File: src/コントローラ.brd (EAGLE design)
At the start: 100 x 80 mm, 13 parts, among them SW1 TOGGLESWITCH

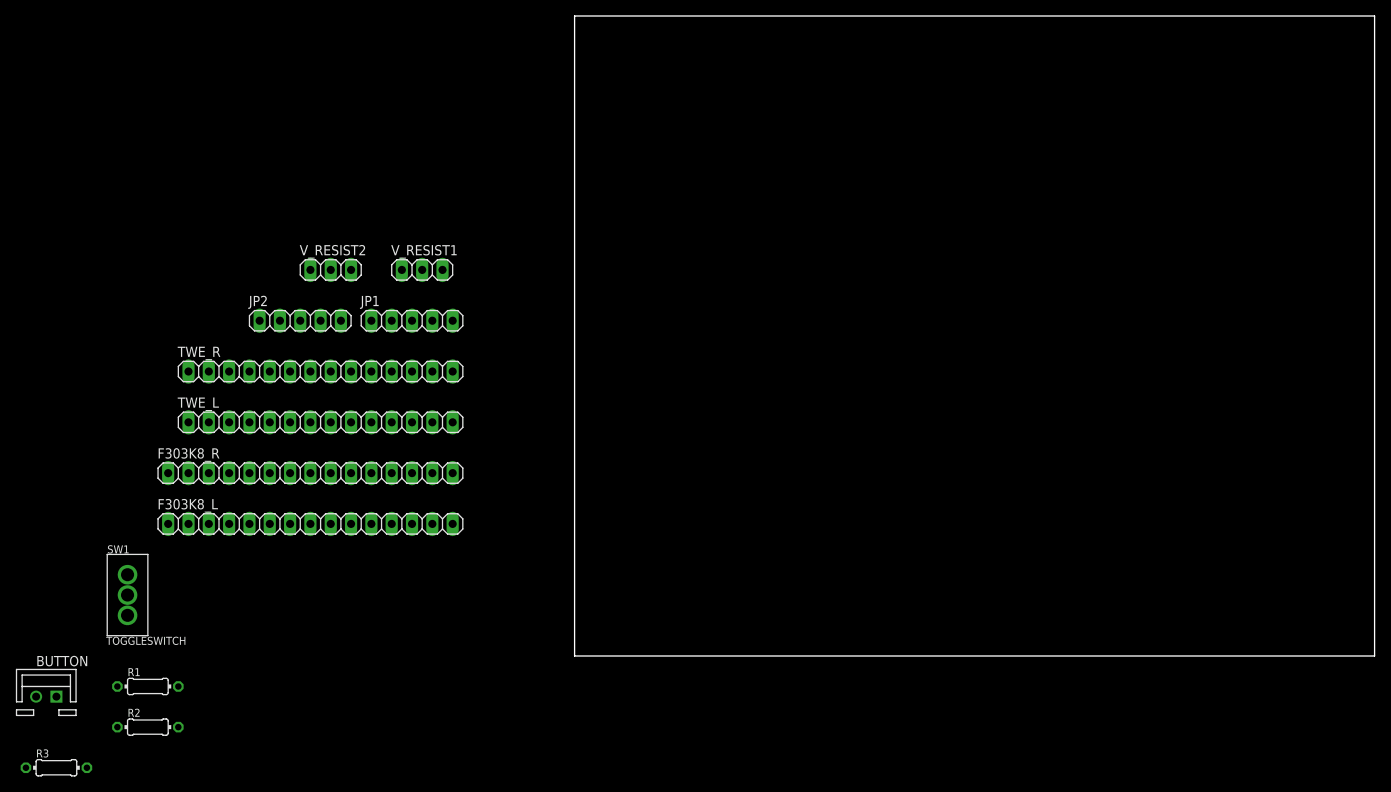
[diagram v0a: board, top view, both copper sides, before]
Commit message: [add]コントローラー.brdの追加
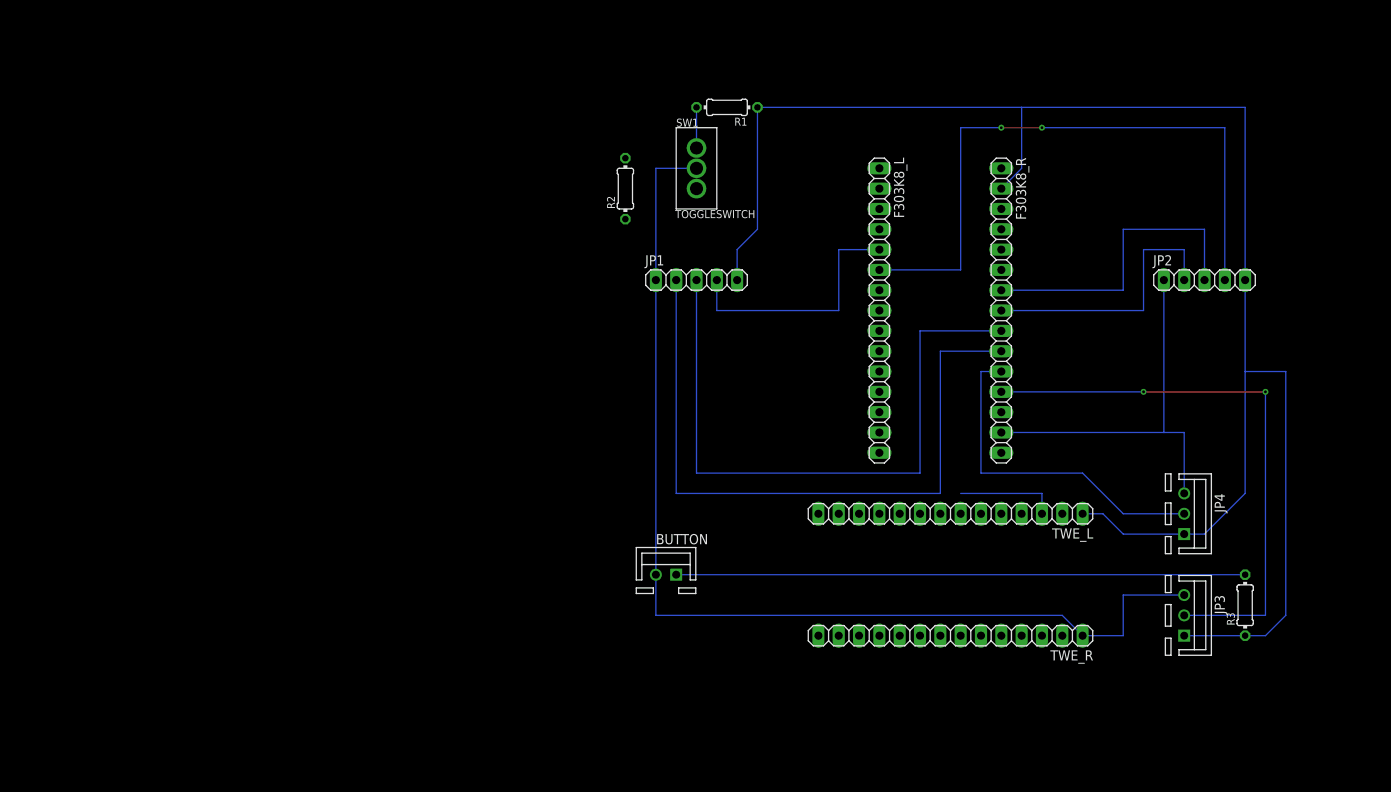
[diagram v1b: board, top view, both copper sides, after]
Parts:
- removed V_RESIST1, V_RESIST2: (no value), pinhead:1X03
- added JP3, JP4: (no value), con-jst-xh:B3B-XH
- added U$1: (no value), prototyping-board:TYPE.B
- moved R3 150.0 mm to (83.8, 6.35), turned to 90 degrees
- moved JP2 113.1 mm to (78.7, 47.0)
- moved R1 102.4 mm to (19.1, 68.6), turned to 180 degrees
- moved R2 90.0 mm to (6.35, 58.4), turned to 90 degrees
- moved SW1 88.9 mm to (15.2, 61.0)
- moved F303K8_R 88.7 mm to (53.3, 43.2), turned to 270 degrees
- moved TWE_R 85.4 mm to (47.0, 2.54), turned to 180 degrees
- moved TWE_L 79.6 mm to (47.0, 17.8), turned to 180 degrees
- moved BUTTON 79.0 mm to (11.4, 10.2)
- moved F303K8_L 76.0 mm to (38.1, 43.2), turned to 270 degrees
- moved JP1 35.9 mm to (15.2, 47.0)
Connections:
- net 3V3: now also JP3.3, JP4.3; no longer V_RESIST1.1, V_RESIST2.1
- net BT_IN: now also F303K8_L.9
- net GND: now also JP3.1, JP4.1; no longer V_RESIST1.3, V_RESIST2.3
- net SW_DOWN: now also F303K8_L.11
- net SW_UP: now also F303K8_L.10
- net VR_IN1: now also JP3.2; no longer V_RESIST1.2
- net VR_IN2: now also JP4.2; no longer V_RESIST2.2
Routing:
- net GND: track 0.00 -> 215.9 mm
- net 3V3: track 0.00 -> 182.7 mm
- net VERT1: track 0.00 -> 85.1 mm
- net SEL2: track 0.00 -> 80.0 mm, vias 0 -> 2
- net HORZ1: track 0.00 -> 80.0 mm
- net VR_IN1: track 0.00 -> 71.1 mm, vias 0 -> 2
- net BT_IN: track 0.00 -> 71.1 mm
- net VR_IN2: track 0.00 -> 42.7 mm
- net HORZ2: track 0.00 -> 39.4 mm
- net VERT2: track 0.00 -> 34.3 mm
- net SEL1: track 0.00 -> 31.8 mm
- net TX: track 0.00 -> 12.7 mm
- net SW_UP: track 0.00 -> 5.08 mm
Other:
- board outline removed

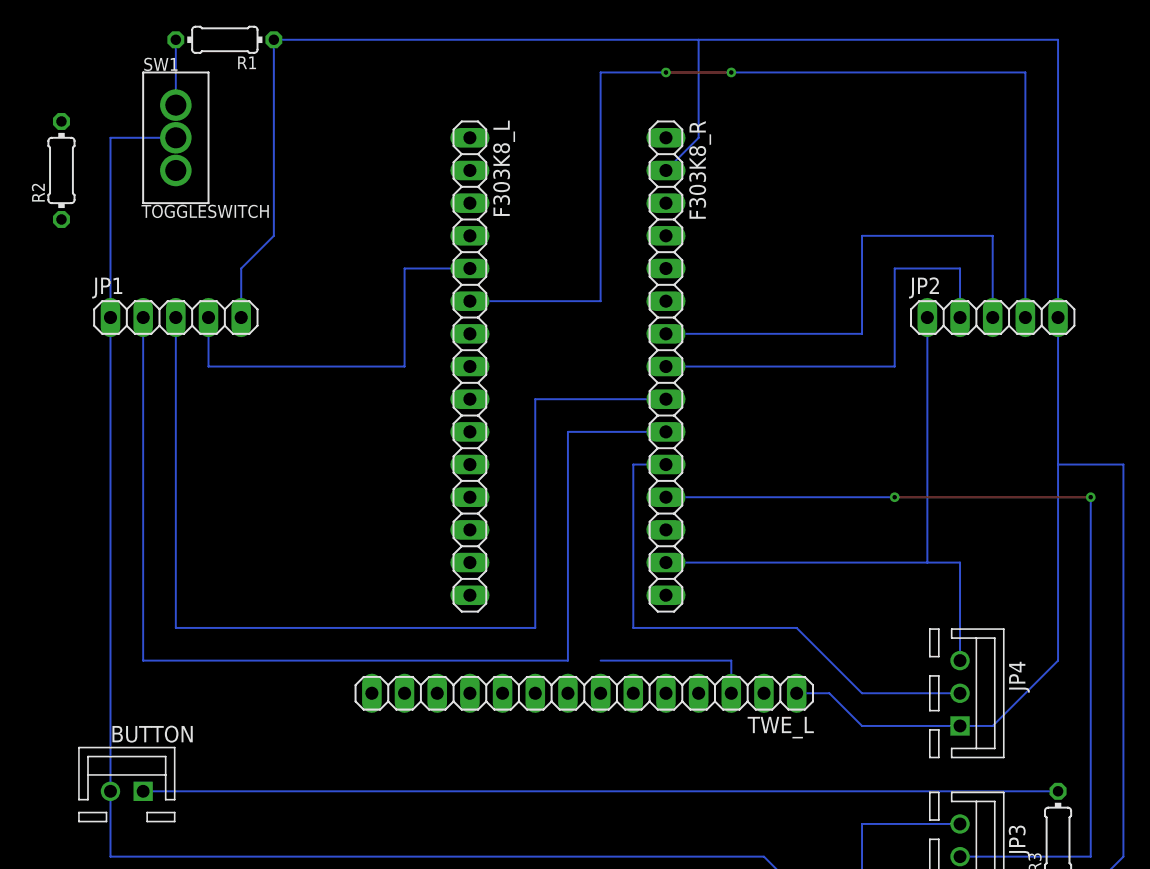
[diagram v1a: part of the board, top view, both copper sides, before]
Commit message: [fix]コントローラー.brdの修正
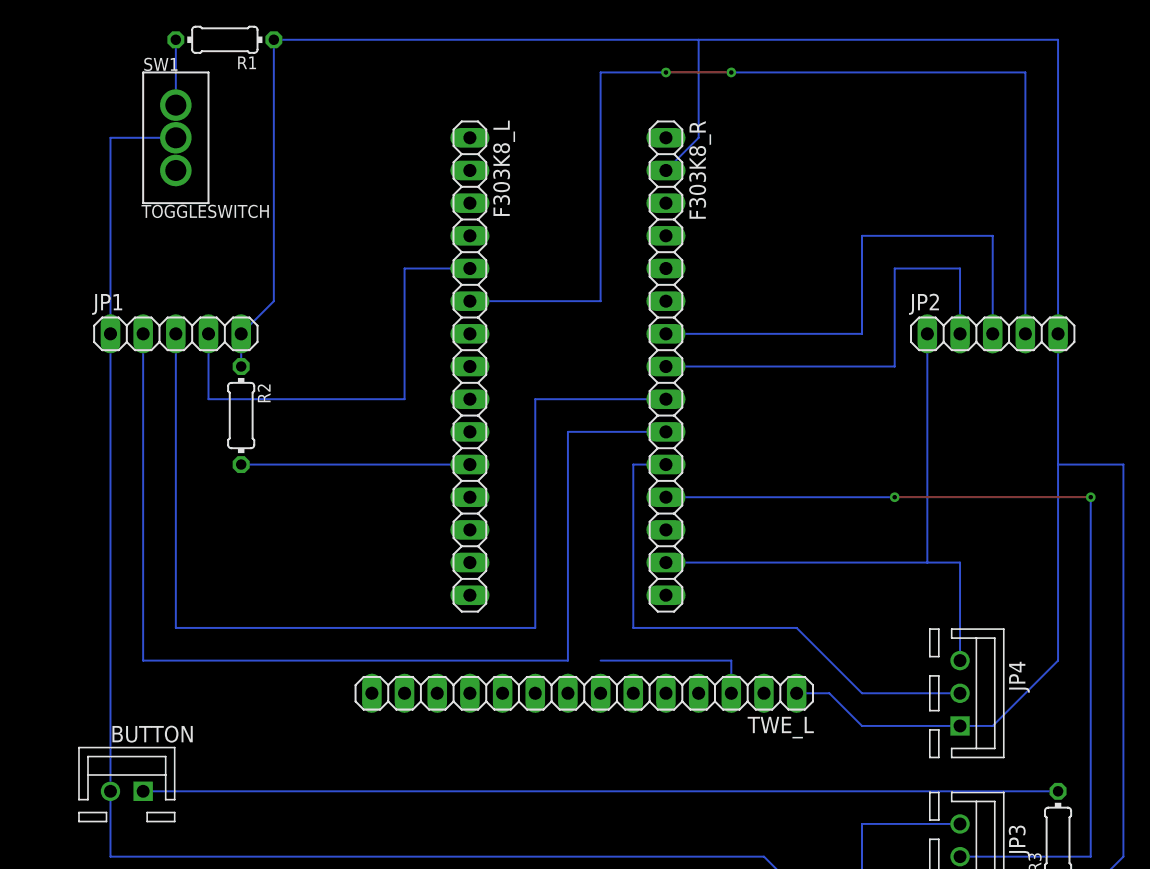
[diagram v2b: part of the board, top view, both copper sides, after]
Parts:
- moved R2 23.6 mm to (20.3, 39.4), turned to 270 degrees
- moved JP1 1.27 mm to (15.2, 45.7)
- moved JP2 1.27 mm to (78.7, 45.7)
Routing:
- net SW_DOWN: track 0.00 -> 17.8 mm
- net SEL1: track 31.8 -> 35.6 mm
- net GND: track 215.9 -> 219.7 mm
- net VERT1: track 85.1 -> 83.8 mm
- net 3V3: track 182.7 -> 181.4 mm
- net VERT2: track 34.3 -> 35.6 mm
- net HORZ2: track 39.4 -> 40.6 mm
- net SEL2: track 80.0 -> 81.3 mm
- net HORZ1: track 80.0 -> 78.7 mm
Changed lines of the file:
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@@
 <attribute name="VALUE" x="50.165" y="62.23" size="1.27" layer="27" rot="R270"/>
 </element>
-<element name="JP1" library="pinhead" library_urn="urn:adsk.eagle:library:325" package="1X05" package3d_urn="urn:adsk.eagle:package:22469/2" value="" x="15.24" y="46.99" smashed="yes">
-<attribute name="NAME" x="8.8138" y="48.8188" size="1.27" layer="25" ratio="10"/>
-<attribute name="POPULARITY" value="69" x="35.56" y="5.08" size="1.778" layer="27" display="off"/>
-<attribute name="VALUE" x="8.89" y="43.815" size="1.27" layer="27"/>
-</element>
-<element name="JP2" library="pinhead" library_urn="urn:adsk.eagle:library:325" package="1X05" package3d_urn="urn:adsk.eagle:package:22469/2" value="" x="78.74" y="46.99" smashed="yes">
-<attribute name="NAME" x="72.3138" y="48.8188" size="1.27" layer="25" ratio="10"/>
-<attribute name="POPULARITY" value="69" x="113.03" y="5.08" size="1.778" layer="27" display="off"/>
-<attribute name="VALUE" x="72.39" y="43.815" size="1.27" layer="27"/>
+<element name="JP1" library="pinhead" library_urn="urn:adsk.eagle:library:325" package="1X05" package3d_urn="urn:adsk.eagle:package:22469/2" value="" x="15.24" y="45.72" smashed="yes">
+<attribute name="NAME" x="8.8138" y="47.5488" size="1.27" layer="25" ratio="10"/>
+<attribute name="POPULARITY" value="69" x="35.56" y="3.81" size="1.778" layer="27" display="off"/>
+<attribute name="VALUE" x="8.89" y="42.545" size="1.27" layer="27"/>
+</element>
+<element name="JP2" library="pinhead" library_urn="urn:adsk.eagle:library:325" package="1X05" package3d_urn="urn:adsk.eagle:package:22469/2" value="" x="78.74" y="45.72" smashed="yes">
+<attribute name="NAME" x="72.3138" y="47.5488" size="1.27" layer="25" ratio="10"/>
+<attribute name="POPULARITY" value="69" x="113.03" y="3.81" size="1.778" layer="27" display="off"/>
+<attribute name="VALUE" x="72.39" y="42.545" size="1.27" layer="27"/>
 </element>
 <element name="TWE_L" library="pinhead" library_urn="urn:adsk.eagle:library:325" package="1X14" package3d_urn="urn:adsk.eagle:package:22417/2" value="" x="46.99" y="17.78" smashed="yes" rot="R180">
@@
 <attribute name="VALUE" x="20.6756" y="69.0626" size="0.9906" layer="27" ratio="10" rot="R180"/>
 </element>
-<element name="R2" library="rcl" library_urn="urn:adsk.eagle:library:334" package="0204/7" package3d_urn="urn:adsk.eagle:package:23498/2" value="10k" x="6.35" y="58.42" smashed="yes" rot="R90">
-<attribute name="NAME" x="5.0546" y="55.88" size="0.9906" layer="25" ratio="10" rot="R90"/>
-<attribute name="POPULARITY" value="79" x="6.35" y="58.42" size="1.778" layer="27" rot="R90" display="off"/>
-<attribute name="SPICEPREFIX" value="R" x="6.35" y="58.42" size="1.778" layer="27" rot="R90" display="off"/>
-<attribute name="VALUE" x="6.8326" y="56.7944" size="0.9906" layer="27" ratio="10" rot="R90"/>
+<element name="R2" library="rcl" library_urn="urn:adsk.eagle:library:334" package="0204/7" package3d_urn="urn:adsk.eagle:package:23498/2" value="10k" x="20.32" y="39.37" smashed="yes" rot="R270">
+<attribute name="NAME" x="21.6154" y="41.91" size="0.9906" layer="25" ratio="10" rot="R270"/>
+<attribute name="POPULARITY" value="79" x="20.32" y="39.37" size="1.778" layer="27" rot="R270" display="off"/>
+<attribute name="SPICEPREFIX" value="R" x="20.32" y="39.37" size="1.778" layer="27" rot="R270" display="off"/>
+<attribute name="VALUE" x="19.8374" y="40.9956" size="0.9906" layer="27" ratio="10" rot="R270"/>
 </element>
 <element name="BUTTON" library="con-jst-xh" package="B2B-XH" value="02-JST" x="11.43" y="10.16" smashed="yes">
@@
 <wire x1="83.82" y1="20.32" x2="78.74" y2="15.24" width="0.1524" layer="16"/>
 <wire x1="78.74" y1="15.24" x2="76.2" y2="15.24" width="0.1524" layer="16"/>
-<wire x1="22.86" y1="68.58" x2="22.86" y2="53.34" width="0.1524" layer="16"/>
-<wire x1="22.86" y1="53.34" x2="20.32" y2="50.8" width="0.1524" layer="16"/>
-<wire x1="20.32" y1="50.8" x2="20.32" y2="46.99" width="0.1524" layer="16"/>
 <wire x1="22.86" y1="68.58" x2="55.88" y2="68.58" width="0.1524" layer="16"/>
 <wire x1="55.88" y1="68.58" x2="83.82" y2="68.58" width="0.1524" layer="16"/>
-<wire x1="83.82" y1="68.58" x2="83.82" y2="46.99" width="0.1524" layer="16"/>
+<wire x1="83.82" y1="68.58" x2="83.82" y2="45.72" width="0.1524" layer="16"/>
 <wire x1="53.34" y1="58.42" x2="55.88" y2="60.96" width="0.1524" layer="16"/>
 <wire x1="55.88" y1="60.96" x2="55.88" y2="68.58" width="0.1524" layer="16"/>
@@
 <wire x1="88.9" y1="5.08" x2="88.9" y2="35.56" width="0.1524" layer="16"/>
 <wire x1="88.9" y1="35.56" x2="83.82" y2="35.56" width="0.1524" layer="16"/>
-<wire x1="83.82" y1="46.99" x2="83.82" y2="35.56" width="0.1524" layer="16"/>
-<wire x1="6.35" y1="54.61" x2="20.32" y2="46.99" width="0" layer="19" extent="1-1"/>
+<wire x1="83.82" y1="45.72" x2="83.82" y2="35.56" width="0.1524" layer="16"/>
+<wire x1="20.32" y1="45.72" x2="20.32" y2="43.18" width="0.1524" layer="16"/>
+<wire x1="20.32" y1="45.72" x2="22.86" y2="48.26" width="0.1524" layer="16"/>
+<wire x1="22.86" y1="48.26" x2="22.86" y2="68.58" width="0.1524" layer="16"/>
 </signal>
 <signal name="3V3">
@@
 <contactref element="JP3" pad="3"/>
 <contactref element="JP4" pad="3"/>
-<wire x1="10.16" y1="10.16" x2="10.16" y2="46.99" width="0.1524" layer="16"/>
-<wire x1="10.16" y1="46.99" x2="10.16" y2="60.96" width="0.1524" layer="16"/>
+<wire x1="10.16" y1="10.16" x2="10.16" y2="45.72" width="0.1524" layer="16"/>
+<wire x1="10.16" y1="45.72" x2="10.16" y2="60.96" width="0.1524" layer="16"/>
 <wire x1="10.16" y1="60.96" x2="15.24" y2="60.96" width="0.1524" layer="16"/>
 <wire x1="76.2" y1="20.32" x2="76.2" y2="27.94" width="0.1524" layer="16"/>
 <wire x1="76.2" y1="27.94" x2="73.66" y2="27.94" width="0.1524" layer="16"/>
 <wire x1="73.66" y1="27.94" x2="53.34" y2="27.94" width="0.1524" layer="16"/>
-<wire x1="73.66" y1="46.99" x2="73.66" y2="27.94" width="0.1524" layer="16"/>
+<wire x1="73.66" y1="45.72" x2="73.66" y2="27.94" width="0.1524" layer="16"/>
 <wire x1="63.5" y1="2.54" x2="68.58" y2="2.54" width="0.1524" layer="16"/>
 <wire x1="68.58" y1="2.54" x2="68.58" y2="7.62" width="0.1524" layer="16"/>
@@
 <wire x1="71.12" y1="43.18" x2="71.12" y2="50.8" width="0.1524" layer="16"/>
 <wire x1="71.12" y1="50.8" x2="76.2" y2="50.8" width="0.1524" layer="16"/>
-<wire x1="76.2" y1="50.8" x2="76.2" y2="46.99" width="0.1524" layer="16"/>
+<wire x1="76.2" y1="50.8" x2="76.2" y2="45.72" width="0.1524" layer="16"/>
 </signal>
 <signal name="HORZ2">
@@
 <wire x1="68.58" y1="45.72" x2="68.58" y2="53.34" width="0.1524" layer="16"/>
 <wire x1="68.58" y1="53.34" x2="78.74" y2="53.34" width="0.1524" layer="16"/>
-<wire x1="78.74" y1="53.34" x2="78.74" y2="46.99" width="0.1524" layer="16"/>
+<wire x1="78.74" y1="53.34" x2="78.74" y2="45.72" width="0.1524" layer="16"/>
 </signal>
 <signal name="SEL2">
 <contactref element="JP2" pad="4"/>
 <contactref element="F303K8_L" pad="6"/>
-<wire x1="81.28" y1="46.99" x2="81.28" y2="66.04" width="0.1524" layer="16"/>
+<wire x1="81.28" y1="45.72" x2="81.28" y2="66.04" width="0.1524" layer="16"/>
 <wire x1="81.28" y1="66.04" x2="58.42" y2="66.04" width="0.1524" layer="16"/>
 <via x="58.42" y="66.04" extent="1-16" drill="0.35"/>
@@
 <contactref element="JP1" pad="2"/>
 <contactref element="F303K8_R" pad="10"/>
-<wire x1="12.7" y1="46.99" x2="12.7" y2="20.32" width="0.1524" layer="16"/>
+<wire x1="12.7" y1="45.72" x2="12.7" y2="20.32" width="0.1524" layer="16"/>
 <wire x1="12.7" y1="20.32" x2="45.72" y2="20.32" width="0.1524" layer="16"/>
 <wire x1="45.72" y1="20.32" x2="45.72" y2="38.1" width="0.1524" layer="16"/>
@@
 <contactref element="JP1" pad="3"/>
 <contactref element="F303K8_R" pad="9"/>
-<wire x1="15.24" y1="46.99" x2="15.24" y2="22.86" width="0.1524" layer="16"/>
+<wire x1="15.24" y1="45.72" x2="15.24" y2="22.86" width="0.1524" layer="16"/>
 <wire x1="15.24" y1="22.86" x2="43.18" y2="22.86" width="0.1524" layer="16"/>
 <wire x1="43.18" y1="22.86" x2="43.18" y2="40.64" width="0.1524" layer="16"/>
@@
 <contactref element="JP1" pad="4"/>
 <contactref element="F303K8_L" pad="5"/>
-<wire x1="17.78" y1="46.99" x2="17.78" y2="43.18" width="0.1524" layer="16"/>
-<wire x1="17.78" y1="43.18" x2="33.02" y2="43.18" width="0.1524" layer="16"/>
-<wire x1="33.02" y1="43.18" x2="33.02" y2="50.8" width="0.1524" layer="16"/>
+<wire x1="17.78" y1="45.72" x2="17.78" y2="40.64" width="0.1524" layer="16"/>
+<wire x1="17.78" y1="40.64" x2="33.02" y2="40.64" width="0.1524" layer="16"/>
+<wire x1="33.02" y1="40.64" x2="33.02" y2="50.8" width="0.1524" layer="16"/>
 <wire x1="33.02" y1="50.8" x2="38.1" y2="50.8" width="0.1524" layer="16"/>
 </signal>
@@
 <contactref element="R2" pad="2"/>
 <contactref element="F303K8_L" pad="11"/>
-<wire x1="38.1" y1="35.56" x2="6.35" y2="62.23" width="0" layer="19" extent="1-1"/>
-<wire x1="15.24" y1="58.42" x2="38.1" y2="35.56" width="0" layer="19" extent="1-1"/>
+<wire x1="20.32" y1="35.56" x2="38.1" y2="35.56" width="0.1524" layer="16"/>
+<wire x1="20.32" y1="35.56" x2="15.24" y2="58.42" width="0" layer="19" extent="1-1"/>
 </signal>
 <signal name="BT_IN">

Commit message: [add]メイン回路
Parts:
- moved F303K8_L 2.54 mm to (38.1, 45.7)
- moved F303K8_R 2.54 mm to (53.3, 45.7)
- moved JP1 2.54 mm to (15.2, 48.3)
- moved R2 2.54 mm to (20.3, 41.9)
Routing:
- net BT_IN: track 71.1 -> 129.5 mm, vias 0 -> 2
- net SW_UP: track 5.08 -> 50.8 mm, vias 0 -> 2
- net TX: track 12.7 -> 48.3 mm, vias 0 -> 2
- net RX: track 0.00 -> 33.0 mm, vias 0 -> 2
- net SW_DOWN: track 17.8 -> 45.7 mm, vias 0 -> 2
- net 3V3: track 181.4 -> 204.3 mm, vias 0 -> 2
- net GND: track 219.7 -> 224.3 mm
- net SEL2: track 81.3 -> 78.7 mm
- net VR_IN2: track 42.7 -> 45.3 mm
- net VERT2: track 35.6 -> 33.0 mm
- net HORZ2: track 40.6 -> 38.1 mm
- net VR_IN1: track 71.1 -> 73.7 mm

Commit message: fix
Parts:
- added BUTTON2: 02-JST, con-jst-xh:B2B-XH
- added KAHEN: (no value), pinhead:1X03
- added R4, R5, R6: 10k, rcl:0204/7
- added R7, R8, R9: (no value), rcl:0207/7
- added SLIDESWITCH: SLEDESWITCH, slide switch:SLIDESWITCH
- added SW2: TOGGLESWITCH, ToggleSwitch:TOGGLESWITCH
- moved R3 83.9 mm to (3.81, -19.1), turned to 0 degrees
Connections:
- net SW_DOWN renamed SW_DOWN1
- net SW_UP renamed SW_UP1
- removed net BT_IN: BUTTON.1, F303K8_L.9, R3.2
- new net BT_IN1: BUTTON.1, F303K8_L.9, R5.2
- new net BT_IN2: F303K8_L.14, R6.2
- new net CONNECT: SLIDESWITCH.1
- new net CONNECT1: SLIDESWITCH.2
- new net N$1: R7.2, SLIDESWITCH.5
- new net N$2: R8.2, SLIDESWITCH.6
- new net N$5: KAHEN.2
- new net N$7: R9.1
- new net RT_IN2: BUTTON2.1
- new net SW_DOWN2: F303K8_L.13, R4.2, SW2.D
- new net SW_UP2: F303K8_L.12, R3.2, SW2.U
- new net SYUUDOUSI＋: R9.2
- net 3V3: now also BUTTON2.2, KAHEN.3, SLIDESWITCH.3, SLIDESWITCH.4, SW2.M
- net GND: now also KAHEN.1, R4.1, R5.1, R6.1, R7.1, R8.1
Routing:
- net BT_IN: track 129.5 -> 0.00 mm, vias 2 -> 0
- net BT_IN1: track 0.00 -> 119.4 mm, vias 0 -> 2
